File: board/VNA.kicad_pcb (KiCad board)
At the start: 2 copper layers, 100 x 100 mm, 113 parts, among them J1 Conn_01x08, J10 Conn_01x01, J11 Conn_01x01, J12 Conn_01x01, J13 Barrel_Jack, J15 Conn_02x05_Odd_Even, J17 Conn_01x04, J18 Conn_01x01, J19 Conn_01x01, J2 Conn_Coaxial, J20 Conn_01x01, J21 Conn_01x01, J22 Conn_01x02, J3 Conn_01x01, J4 Conn_01x01, J5 Conn_01x01, J6 Conn_01x01, J7 Conn_01x01, J8 Conn_01x01, J9 Conn_Coaxial, U1 SI5351A, U2 74HC14, U3 SA612, U4 SA612, U5 SA612, U6 TL082, U7 TL082, U9 LM7805_TO220, Y1 27 MHz

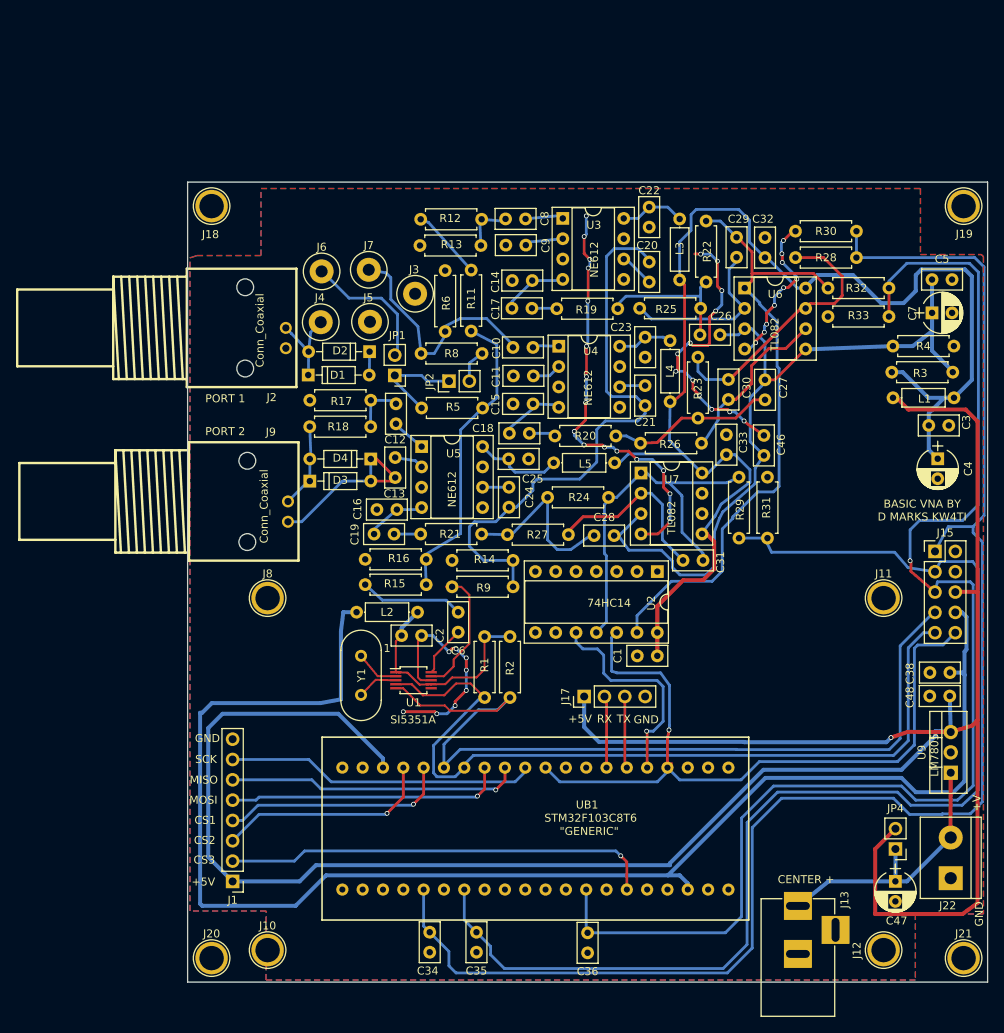
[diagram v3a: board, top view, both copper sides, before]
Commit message: Substitute LM339 for 74HC14
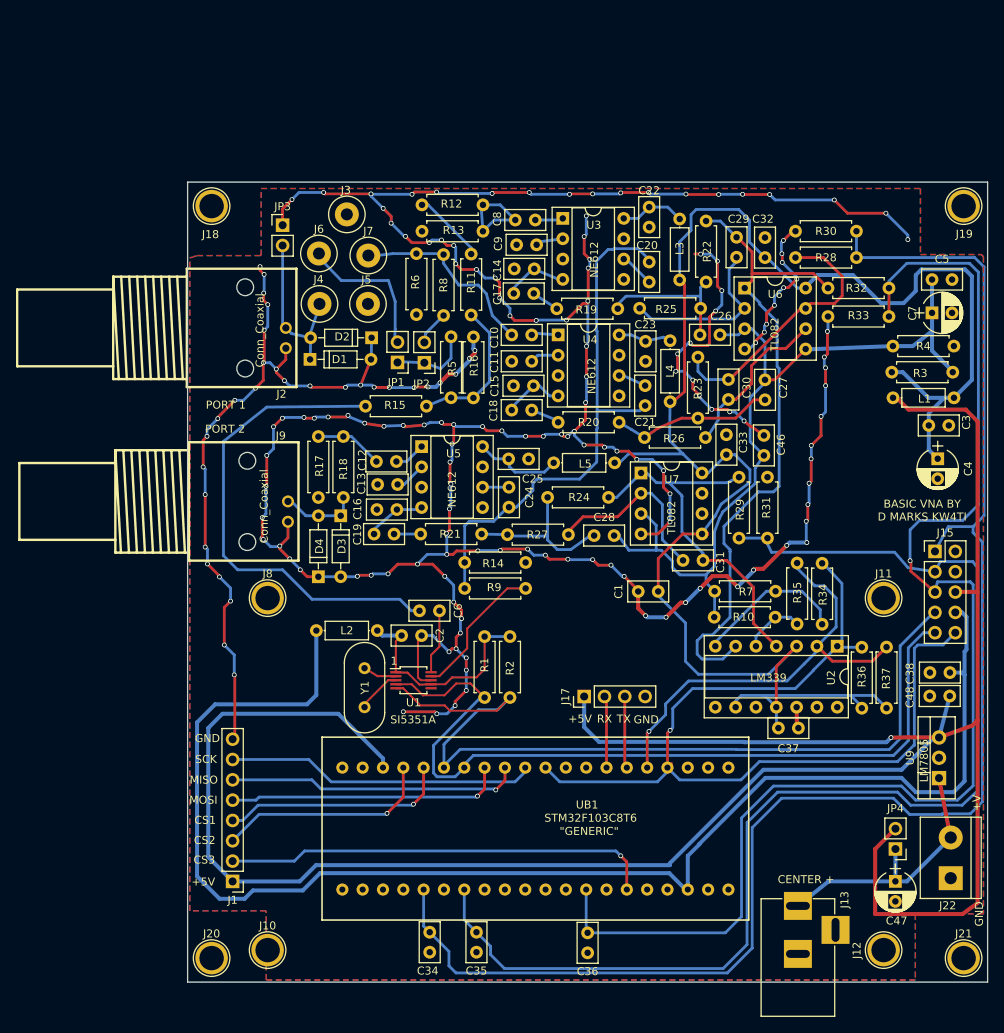
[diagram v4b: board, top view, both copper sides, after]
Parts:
- added C37: 100 nF, Capacitors_THT:C_Disc_D5.0mm_W2.5mm_P2.50mm, F.Cu at (126.3, 118.2)
- added JP3: Jumper_NC_Small, Pin_Headers:Pin_Header_Straight_1x02_Pitch2.54mm, F.Cu at (61.9, 55.4)
- added R10: 10k, Resistors_THT:R_Axial_DIN0207_L6.3mm_D2.5mm_P7.62mm_Horizontal, F.Cu at (123.4, 104.4)
- added R34: 1M, Resistors_THT:R_Axial_DIN0207_L6.3mm_D2.5mm_P7.62mm_Horizontal, F.Cu at (129.3, 105.3)
- added R35: 1M, Resistors_THT:R_Axial_DIN0207_L6.3mm_D2.5mm_P7.62mm_Horizontal, F.Cu at (126.2, 105.2)
- added R36: 1k, Resistors_THT:R_Axial_DIN0207_L6.3mm_D2.5mm_P7.62mm_Horizontal, F.Cu at (134.3, 108.1)
- added R37: 1k, Resistors_THT:R_Axial_DIN0207_L6.3mm_D2.5mm_P7.62mm_Horizontal, F.Cu at (137.4, 108.1)
- added R7: 10k, Resistors_THT:R_Axial_DIN0207_L6.3mm_D2.5mm_P7.62mm_Horizontal, F.Cu at (123.5, 101.1)
- U2: value 74HC14 -> LM339
- moved U2 24.4 mm to (131.2, 108.0)
- moved R15 22.3 mm to (79.9, 78.0)
- moved R16 21.0 mm to (85.7, 77.0), turned to 90 degrees
- moved D4 16.1 mm to (66.3, 99.3), turned to 90 degrees
- moved J3 13.1 mm to (69.9, 54.0)
- moved R8 12.7 mm to (82.0, 59.1), turned to 270 degrees
- moved R6 10.4 mm to (78.6, 58.9), turned to 270 degrees
- moved R5 9.63 mm to (82.9, 69.3), turned to 270 degrees
- moved R14 9.20 mm to (92.3, 97.5), turned to 180 degrees
- moved C1 8.05 mm to (108.8, 101.2)
- moved R17 7.97 mm to (66.3, 81.8), turned to 270 degrees
- moved R9 6.05 mm to (84.6, 100.8), turned to 0 degrees
- moved D3 5.80 mm to (69.1, 91.7), turned to 270 degrees
- moved L2 5.53 mm to (73.7, 106.1)
- moved C6 4.84 mm to (79.0, 103.6), turned to 0 degrees
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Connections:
- U2 pad 1: GND -> SYNCSAMPLE
- U2 pad 10: SYNCSAMPLE2 -> GND
- U2 pad 11: Net-(C31-Pad1) -> FILT5V
- U2 pad 12: SYNCSAMPLE -> GND
- U2 pad 13: Net-(C29-Pad1) -> (no net)
- U2 pad 14: FILT5V -> (no net)
- U2 pad 2: (no net) -> SYNCSAMPLE2
- U2 pad 3: GND -> FILT5V
- U2 pad 4: (no net) -> Net-(C31-Pad1)
- U2 pad 5: GND -> Net-(R10-Pad1)
- U2 pad 6: (no net) -> Net-(C29-Pad1)
- U2 pad 7: GND -> Net-(R34-Pad1)
- U2 pad 8: (no net) -> GND
- U2 pad 9: GND -> FILT5V
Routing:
- net GND: track 163.1 -> 570.9 mm, vias 45 -> 172
- net FILT5V: track 168.4 -> 223.5 mm
- net Net-(C6-Pad1): track 13.0 -> 60.9 mm
- net SYNCSAMPLE2: track 27.2 -> 55.5 mm
- net SYNCSAMPLE: track 93.4 -> 116.1 mm
- net CLK0: track 39.2 -> 19.3 mm
- net Net-(R34-Pad1): track 0.00 -> 19.1 mm
- net Net-(D1-Pad1): track 11.3 -> 21.0 mm
- net +3V3: track 186.1 -> 177.5 mm
- net Net-(R10-Pad1): track 0.00 -> 7.72 mm
- net 2V5: track 98.1 -> 105.7 mm
- net SAMPVOLT: track 6.49 -> 12.9 mm
- net SAMPCUR: track 29.9 -> 24.6 mm
- net CLK1: track 72.8 -> 67.9 mm
- net Net-(C29-Pad1): track 79.4 -> 83.2 mm
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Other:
- board text added: "LM339"
- board text removed: "74HC14"

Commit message: Working 1 and 2 port calibration
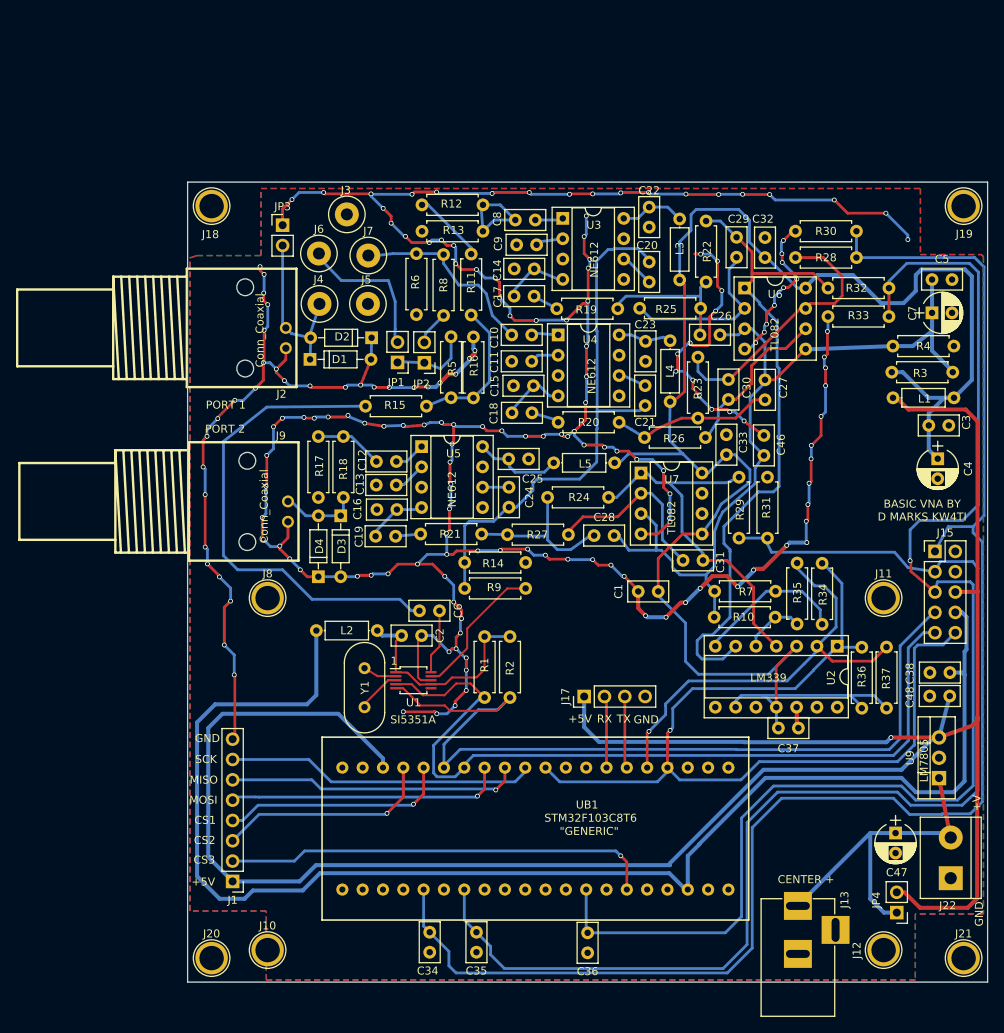
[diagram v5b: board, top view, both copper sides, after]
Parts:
- moved JP4 7.95 mm to (138.6, 141.3)
- moved C47 6.04 mm to (138.5, 131.4)
- moved C18 0.34 mm to (93.0, 78.8)
- moved C19 0.34 mm to (76.0, 94.3)
- moved C17 0.34 mm to (93.3, 64.3)
- moved C13 0.19 mm to (76.1, 87.9)
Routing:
- net +5V: track 304.4 -> 290.6 mm
- net Net-(C47-Pad1): track 34.4 -> 43.3 mm

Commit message: JLCPCB order 2018-12-01
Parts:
- removed JP2: Jumper_NC_Small, Pin_Headers:Pin_Header_Straight_1x02_Pitch2.54mm
- added C39: 100 nF, Capacitors_THT:C_Disc_D5.0mm_W2.5mm_P2.50mm, F.Cu at (63.8, 112.9)
- added C40: 100 nF, Capacitors_THT:C_Disc_D5.0mm_W2.5mm_P2.50mm, F.Cu at (113.2, 103.1)
- added Q1: 2N3904, TO_SOT_Packages_THT:TO-92_Molded_Narrow, F.Cu at (71.7, 102.9)
- added R38: 1k, Resistors_THT:R_Axial_DIN0207_L6.3mm_D2.5mm_P7.62mm_Horizontal, F.Cu at (66.6, 109.6)
- added R39: 1k, Resistors_THT:R_Axial_DIN0207_L6.3mm_D2.5mm_P7.62mm_Horizontal, F.Cu at (79.2, 117.9)
- added R40: 51R, Resistors_THT:R_Axial_DIN0207_L6.3mm_D2.5mm_P7.62mm_Horizontal, F.Cu at (72.0, 93.2)
- added R41: 1k, Resistors_THT:R_Axial_DIN0207_L6.3mm_D2.5mm_P7.62mm_Horizontal, F.Cu at (108.8, 85.5)
- JP1: value Jumper_NC_Small -> Jumper_NC_Dual; footprint Pin_Headers:Pin_Header_Straight_1x02_Pitch2.54mm -> Pin_Headers:Pin_Header_Straight_1x03_Pitch2.54mm
- R15: value 0R -> 51R
- moved J9 89.2 mm to (130.3, 50.9), turned to 180 degrees
- moved D4 68.7 mm to (117.9, 53.9), turned to 270 degrees
- moved L4 61.2 mm to (53.1, 91.6), turned to 90 degrees
- moved D3 60.0 mm to (120.9, 61.5), turned to 90 degrees
- moved R30 55.5 mm to (110.3, 109.4), turned to 90 degrees
- moved C12 54.9 mm to (129.2, 71.0), turned to 90 degrees
- moved C16 53.6 mm to (122.3, 68.5), turned to 270 degrees
- moved C13 52.3 mm to (125.6, 71.0), turned to 90 degrees
- moved R17 52.3 mm to (114.6, 61.5), turned to 90 degrees
- moved C21 51.0 mm to (60.6, 96.3), turned to 0 degrees
- moved U5 50.5 mm to (128.9, 74.1), turned to 270 degrees
- moved C19 48.9 mm to (119.0, 71.0), turned to 90 degrees
- moved R18 47.7 mm to (113.8, 64.2), turned to 0 degrees
- moved R28 45.9 mm to (109.9, 98.7)
- moved C23 45.5 mm to (68.0, 95.4)
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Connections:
- C6 pad 2: Net-(C6-Pad2) -> CLK0
- J15 pad 1: DEMODCUR -> DEMODCUR2
- J15 pad 3: DEMODCUR2 -> DEMODCUR
- J15 pad 4: GND -> +5V
- J15 pad 6: +5V -> +3V3
- J15 pad 8: +3V3 -> ATTEN
- JP1 pad 2: Net-(J6-Pad1) -> Net-(JP1-Pad2)
- R15 pad 1: CLK0 -> Net-(C6-Pad1)
- R15 pad 2: Net-(C6-Pad1) -> Net-(R15-Pad2)
- R16 pad 1: CLK0 -> Net-(C6-Pad1)
- R16 pad 2: GND -> Net-(Q1-Pad3)
- R5 pad 1: Net-(JP1-Pad1) -> Net-(JP1-Pad2)
- R8 pad 2: Net-(JP2-Pad2) -> Net-(JP1-Pad1)
- U1 pad 10: Net-(C6-Pad2) -> Net-(R15-Pad2)
- U2 pad 6: Net-(C29-Pad1) -> Net-(R41-Pad1)
- UB1 pad 27: (no net) -> ATTEN
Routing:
- net 2V5: track 105.7 -> 211.1 mm, vias 0 -> 3
- net FILT5V: track 223.5 -> 312.4 mm, vias 0 -> 1
- net ATTEN: track 0.00 -> 83.8 mm, vias 0 -> 2
- net GND: track 570.9 -> 511.4 mm, vias 172 -> 206
- net Net-(C29-Pad1): track 83.2 -> 28.3 mm
- net Net-(C6-Pad1): track 60.9 -> 17.3 mm
- net Net-(R41-Pad1): track 0.00 -> 33.1 mm
- net CLK1: track 67.9 -> 99.1 mm
- net DEMODCUR2: track 153.0 -> 181.4 mm, vias 0 -> 1
- net Net-(C39-Pad1): track 0.00 -> 27.6 mm
- net +5V: track 290.6 -> 308.1 mm
- net Net-(C30-Pad1): track 34.1 -> 17.7 mm
- net CLK0: track 19.3 -> 6.23 mm
- net Net-(J6-Pad1): track 18.5 -> 5.48 mm
- net Net-(C29-Pad2): track 21.8 -> 9.57 mm
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
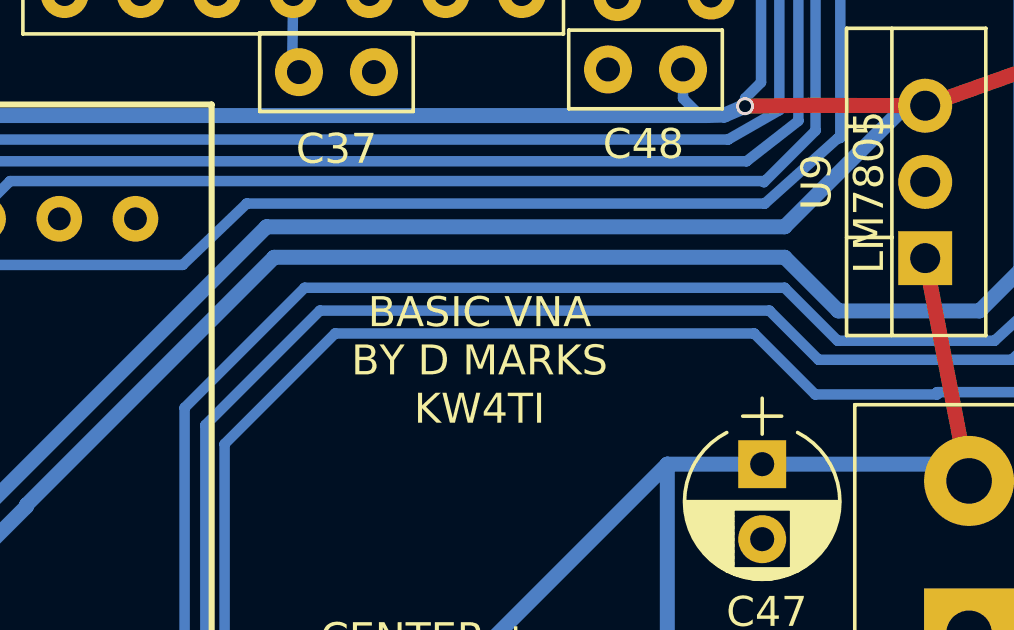
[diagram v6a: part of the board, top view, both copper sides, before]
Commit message: Clarified copyright of PCB, CC-BY-SA 4.0 and code which is zlib
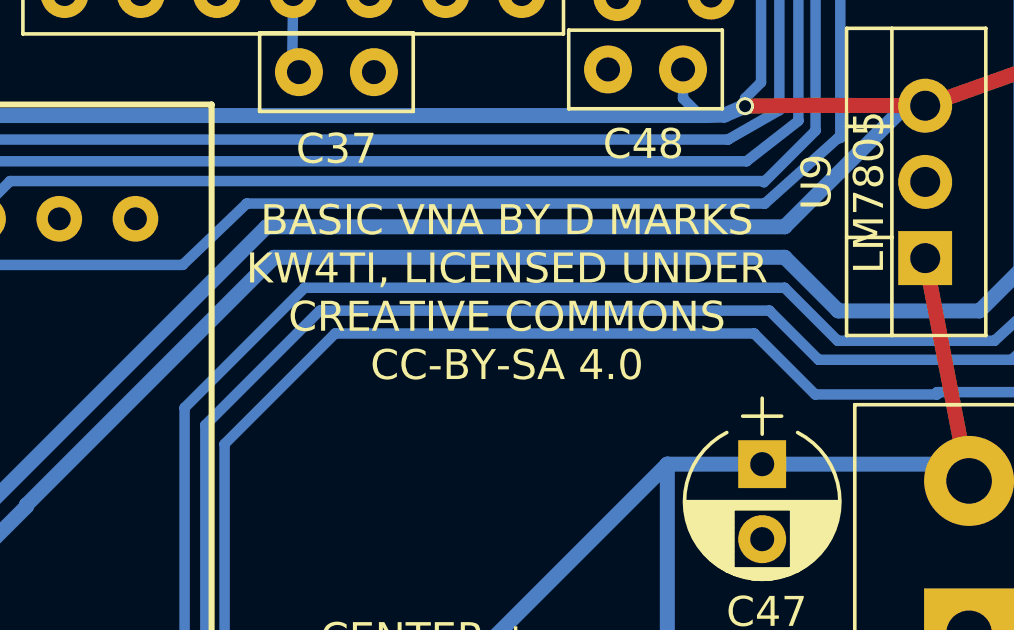
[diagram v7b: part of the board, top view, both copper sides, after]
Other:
- board text added: "BASIC VNA BY D MARKS KW4TI, LICENSED UNDER CREATIVE COMMONS CC-BY-SA 4.0"
- board text removed: "BASIC VNA BY D MARKS KW4TI"
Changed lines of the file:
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@@
     (links 238)
     (no_connects 0)
-    (area 48.252381 29.036639 153.343482 154.699701)
+    (area 49.924999 49.924999 150.075001 150.075001)
     (thickness 1.6)
     (drawings 33)
@@
     (effects (font (size 1 1) (thickness 0.15)))
   )
-  (gr_text "BASIC VNA\nBY D MARKS\nKW4TI" (at 129.07264 127.9144) (layer F.SilkS)
+  (gr_text "BASIC VNA BY D MARKS\nKW4TI, LICENSED UNDER\nCREATIVE COMMONS\nCC-BY-SA 4.0" (at 129.98704 125.6538) (layer F.SilkS)
     (effects (font (size 1 1) (thickness 0.15)))
   )

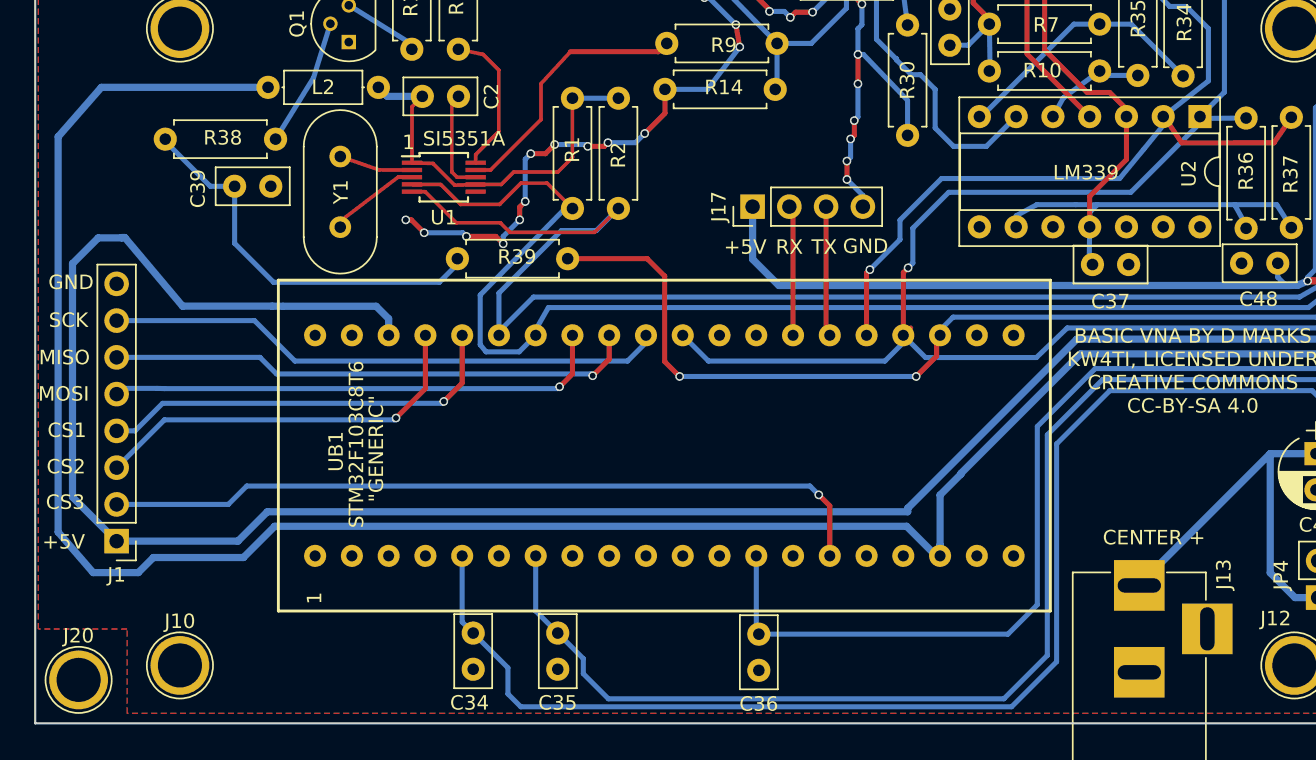
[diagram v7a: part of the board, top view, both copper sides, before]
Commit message: Added some more CS pins to header
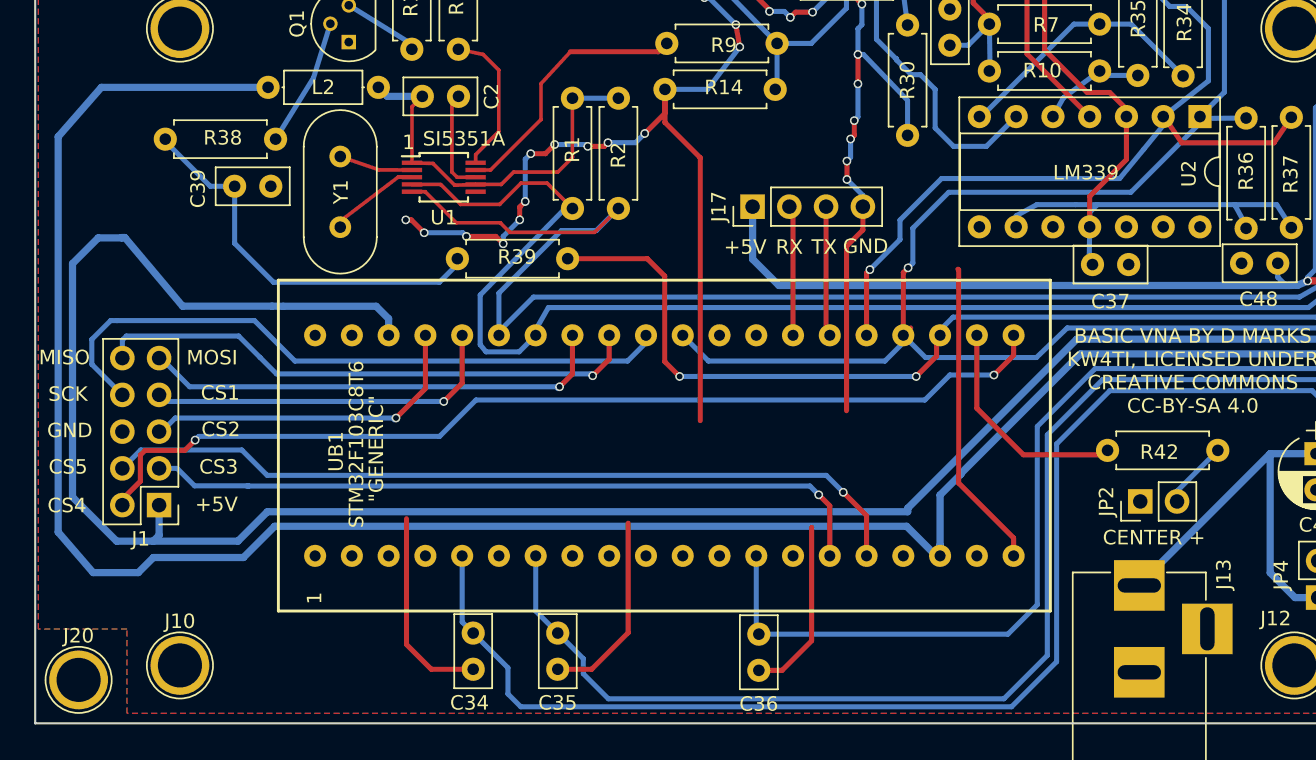
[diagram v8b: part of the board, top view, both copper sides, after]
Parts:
- added JP2: Jumper_NC_Small, Pin_Headers:Pin_Header_Straight_1x02_Pitch2.54mm, F.Cu at (126.4, 134.7)
- added R42: 10k, Resistors_THT:R_Axial_DIN0207_L6.3mm_D2.5mm_P7.62mm_Horizontal, F.Cu at (131.7, 131.1)
- C29, C30, C31: value 100 pF -> 68 pF
- C3: value 10 nF -> 100 nF
- J1: value Conn_01x08 -> Conn_02x05_Odd_Even; footprint Pin_Headers:Pin_Header_Straight_1x08_Pitch2.54mm -> Pin_Headers:Pin_Header_Straight_2x05_Pitch2.54mm
- Q1: value 2N3904 -> SS9018
- R15: value 51R -> 220R
- R16: value 51R -> 100R
- R22, R23, R24: value 68k -> 100k
- R38, R39: value 1k -> 10k
- R40: value 51R -> NC
- moved J1 3.85 mm to (58.6, 134.9)
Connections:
- J1 pad 2: PB10 -> PB12
- J1 pad 3: Net-(J1-Pad3) -> PB10
- J1 pad 4: Net-(J1-Pad4) -> PB11
- J1 pad 6: Net-(J1-Pad6) -> GND
- J1 pad 8: GND -> Net-(J1-Pad8)
- UB1 pad 22: (no net) -> PB11
- UB1 pad 25: (no net) -> PB12
- UB1 pad 26: (no net) -> Net-(R42-Pad2)
- UB1 pad 39: Net-(J1-Pad7) -> Net-(J1-Pad8)
- UB1 pad 40: Net-(J1-Pad6) -> Net-(J1-Pad10)
- UB1 pad 41: Net-(J1-Pad5) -> Net-(J1-Pad9)
- UB1 pad 45: Net-(J1-Pad4) -> Net-(J1-Pad7)
- UB1 pad 46: Net-(J1-Pad3) -> Net-(J1-Pad5)
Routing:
- net GND: track 511.4 -> 610.7 mm
- net PB12: track 0.00 -> 68.5 mm, vias 0 -> 2
- net PB11: track 0.00 -> 56.6 mm, vias 0 -> 1
- net Net-(J1-Pad8): track 0.00 -> 45.8 mm
- net Net-(J1-Pad10): track 0.00 -> 38.3 mm, vias 0 -> 1
- net Net-(J1-Pad6): track 36.7 -> 0.00 mm, vias 1 -> 0
- net Net-(J1-Pad9): track 0.00 -> 32.6 mm, vias 0 -> 1
- net Net-(J1-Pad4): track 28.5 -> 0.00 mm, vias 1 -> 0
- net Net-(J1-Pad3): track 27.3 -> 0.00 mm, vias 1 -> 0
- net Net-(R42-Pad2): track 0.00 -> 15.5 mm
- net Net-(J1-Pad7): track 38.8 -> 25.0 mm, vias 0 -> 1
- net Net-(J1-Pad5): track 34.7 -> 23.5 mm
- net Net-(JP2-Pad2): track 0.00 -> 4.70 mm
- net PB10: track 53.8 -> 51.0 mm
- net +5V: track 308.1 -> 310.8 mm
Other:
- board text added: "CS4"
- board text added: "CS5"
